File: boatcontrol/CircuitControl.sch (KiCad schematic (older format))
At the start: 3 parts, among them SW2601 ESB30, SW2602 ESB30

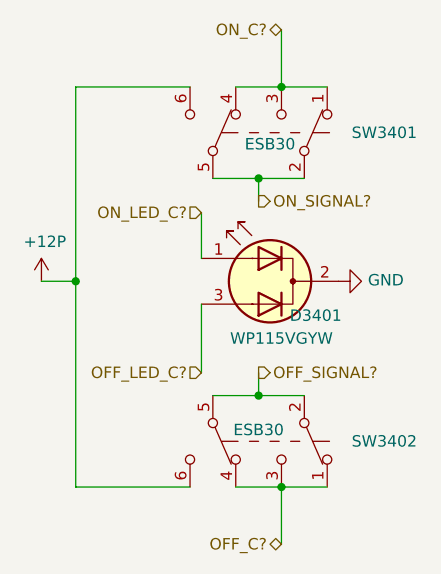
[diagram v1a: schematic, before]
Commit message: Fix extra signals
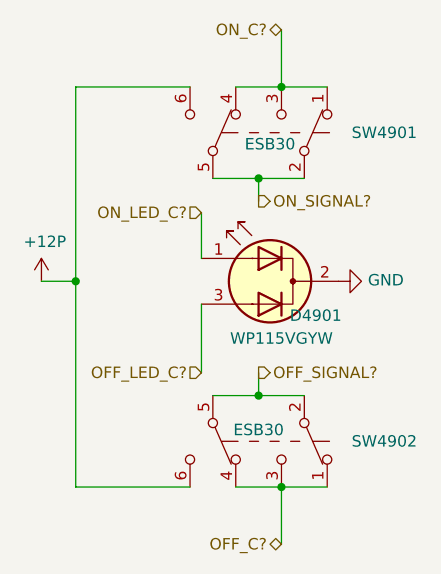
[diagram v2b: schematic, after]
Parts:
- renumbered D2601 to D4101, SW2601 to SW4101, SW2602 to SW4102
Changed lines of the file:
@@
 AR Path="/E0EE2714/E1383403/E15855D9/E150D6D7/E13B21A8" Ref="SW?"  Part="1"
 AR Path="/E0EE2714/E1383403/E15855D9/E150FD51/E13B21A8" Ref="SW?"  Part="1"
-AR Path="/E171B33C/E142CD30/E14BA326/E13B21A8" Ref="SW2602"  Part="1"
-AR Path="/E171B33C/E142CD30/E150AEB9/E13B21A8" Ref="SW2702"  Part="1"
-AR Path="/E171B33C/E142CD30/E150D6D7/E13B21A8" Ref="SW2802"  Part="1"
-AR Path="/E171B33C/E142CD30/E150FD51/E13B21A8" Ref="SW2902"  Part="1"
-AR Path="/E171B33C/E15855D9/E14BA326/E13B21A8" Ref="SW3102"  Part="1"
-AR Path="/E171B33C/E15855D9/E150AEB9/E13B21A8" Ref="SW3202"  Part="1"
-AR Path="/E171B33C/E15855D9/E150D6D7/E13B21A8" Ref="SW3302"  Part="1"
-AR Path="/E171B33C/E15855D9/E150FD51/E13B21A8" Ref="SW3402"  Part="1"
-F 0 "SW3402" V 5750 4250 50  0000 C CNN
+AR Path="/E171B33C/E142CD30/E14BA326/E13B21A8" Ref="SW4102"  Part="1"
+AR Path="/E171B33C/E142CD30/E150AEB9/E13B21A8" Ref="SW4202"  Part="1"
+AR Path="/E171B33C/E142CD30/E150D6D7/E13B21A8" Ref="SW4302"  Part="1"
+AR Path="/E171B33C/E142CD30/E150FD51/E13B21A8" Ref="SW4402"  Part="1"
+AR Path="/E171B33C/E15855D9/E14BA326/E13B21A8" Ref="SW4602"  Part="1"
+AR Path="/E171B33C/E15855D9/E150AEB9/E13B21A8" Ref="SW4702"  Part="1"
+AR Path="/E171B33C/E15855D9/E150D6D7/E13B21A8" Ref="SW4802"  Part="1"
+AR Path="/E171B33C/E15855D9/E150FD51/E13B21A8" Ref="SW4902"  Part="1"
+F 0 "SW4902" V 5750 4250 50  0000 C CNN
 F 1 " ESB30" V 5700 3700 50  0000 C CNN
 F 2 "BoatControl:SW_PUSH_ESB30_DPDT" H 5750 3900 50  0001 C CNN
@@
 AR Path="/E0EE2714/E1383403/E15855D9/E150D6D7/E13B21AE" Ref="#PWR?"  Part="1"
 AR Path="/E0EE2714/E1383403/E15855D9/E150FD51/E13B21AE" Ref="#PWR?"  Part="1"
-AR Path="/E171B33C/E142CD30/E14BA326/E13B21AE" Ref="#PWR02601"  Part="1"
-AR Path="/E171B33C/E142CD30/E150AEB9/E13B21AE" Ref="#PWR02701"  Part="1"
-AR Path="/E171B33C/E142CD30/E150D6D7/E13B21AE" Ref="#PWR02801"  Part="1"
-AR Path="/E171B33C/E142CD30/E150FD51/E13B21AE" Ref="#PWR02901"  Part="1"
-AR Path="/E171B33C/E15855D9/E14BA326/E13B21AE" Ref="#PWR03101"  Part="1"
-AR Path="/E171B33C/E15855D9/E150AEB9/E13B21AE" Ref="#PWR03201"  Part="1"
-AR Path="/E171B33C/E15855D9/E150D6D7/E13B21AE" Ref="#PWR03301"  Part="1"
-AR Path="/E171B33C/E15855D9/E150FD51/E13B21AE" Ref="#PWR03401"  Part="1"
-F 0 "#PWR03401" H 4800 2850 50  0001 C CNN
+AR Path="/E171B33C/E142CD30/E14BA326/E13B21AE" Ref="#PWR04101"  Part="1"
+AR Path="/E171B33C/E142CD30/E150AEB9/E13B21AE" Ref="#PWR04201"  Part="1"
+AR Path="/E171B33C/E142CD30/E150D6D7/E13B21AE" Ref="#PWR04301"  Part="1"
+AR Path="/E171B33C/E142CD30/E150FD51/E13B21AE" Ref="#PWR04401"  Part="1"
+AR Path="/E171B33C/E15855D9/E14BA326/E13B21AE" Ref="#PWR04601"  Part="1"
+AR Path="/E171B33C/E15855D9/E150AEB9/E13B21AE" Ref="#PWR04701"  Part="1"
+AR Path="/E171B33C/E15855D9/E150D6D7/E13B21AE" Ref="#PWR04801"  Part="1"
+AR Path="/E171B33C/E15855D9/E150FD51/E13B21AE" Ref="#PWR04901"  Part="1"
+F 0 "#PWR04901" H 4800 2850 50  0001 C CNN
 F 1 "+12P" H 4815 3173 50  0000 C CNN
 F 2 "" H 4800 3000 50  0001 C CNN
@@
 AR Path="/E0EE2714/E1383403/E15855D9/E150D6D7/E13B21B4" Ref="SW?"  Part="1"
 AR Path="/E0EE2714/E1383403/E15855D9/E150FD51/E13B21B4" Ref="SW?"  Part="1"
-AR Path="/E171B33C/E142CD30/E14BA326/E13B21B4" Ref="SW2601"  Part="1"
-AR Path="/E171B33C/E142CD30/E150AEB9/E13B21B4" Ref="SW2701"  Part="1"
-AR Path="/E171B33C/E142CD30/E150D6D7/E13B21B4" Ref="SW2801"  Part="1"
-AR Path="/E171B33C/E142CD30/E150FD51/E13B21B4" Ref="SW2901"  Part="1"
-AR Path="/E171B33C/E15855D9/E14BA326/E13B21B4" Ref="SW3101"  Part="1"
-AR Path="/E171B33C/E15855D9/E150AEB9/E13B21B4" Ref="SW3201"  Part="1"
-AR Path="/E171B33C/E15855D9/E150D6D7/E13B21B4" Ref="SW3301"  Part="1"
-AR Path="/E171B33C/E15855D9/E150FD51/E13B21B4" Ref="SW3401"  Part="1"
-F 0 "SW3401" V 5750 2900 50  0000 C CNN
+AR Path="/E171B33C/E142CD30/E14BA326/E13B21B4" Ref="SW4101"  Part="1"
+AR Path="/E171B33C/E142CD30/E150AEB9/E13B21B4" Ref="SW4201"  Part="1"
+AR Path="/E171B33C/E142CD30/E150D6D7/E13B21B4" Ref="SW4301"  Part="1"
+AR Path="/E171B33C/E142CD30/E150FD51/E13B21B4" Ref="SW4401"  Part="1"
+AR Path="/E171B33C/E15855D9/E14BA326/E13B21B4" Ref="SW4601"  Part="1"
+AR Path="/E171B33C/E15855D9/E150AEB9/E13B21B4" Ref="SW4701"  Part="1"
+AR Path="/E171B33C/E15855D9/E150D6D7/E13B21B4" Ref="SW4801"  Part="1"
+AR Path="/E171B33C/E15855D9/E150FD51/E13B21B4" Ref="SW4901"  Part="1"
+F 0 "SW4901" V 5750 2900 50  0000 C CNN
 F 1 " ESB30" V 5700 2400 50  0000 C CNN
 F 2 "BoatControl:SW_PUSH_ESB30_DPDT" H 5750 2550 50  0001 C CNN
@@
 AR Path="/E0EE2714/E1383403/E15855D9/E150D6D7/E13B21BC" Ref="D?"  Part="1"
 AR Path="/E0EE2714/E1383403/E15855D9/E150FD51/E13B21BC" Ref="D?"  Part="1"
-AR Path="/E171B33C/E142CD30/E14BA326/E13B21BC" Ref="D2601"  Part="1"
-AR Path="/E171B33C/E142CD30/E150AEB9/E13B21BC" Ref="D2701"  Part="1"
-AR Path="/E171B33C/E142CD30/E150D6D7/E13B21BC" Ref="D2801"  Part="1"
-AR Path="/E171B33C/E142CD30/E150FD51/E13B21BC" Ref="D2901"  Part="1"
-AR Path="/E171B33C/E15855D9/E14BA326/E13B21BC" Ref="D3101"  Part="1"
-AR Path="/E171B33C/E15855D9/E150AEB9/E13B21BC" Ref="D3201"  Part="1"
-AR Path="/E171B33C/E15855D9/E150D6D7/E13B21BC" Ref="D3301"  Part="1"
-AR Path="/E171B33C/E15855D9/E150FD51/E13B21BC" Ref="D3401"  Part="1"
-F 0 "D3401" H 5600 2850 50  0000 C CNN
+AR Path="/E171B33C/E142CD30/E14BA326/E13B21BC" Ref="D4101"  Part="1"
+AR Path="/E171B33C/E142CD30/E150AEB9/E13B21BC" Ref="D4201"  Part="1"
+AR Path="/E171B33C/E142CD30/E150D6D7/E13B21BC" Ref="D4301"  Part="1"
+AR Path="/E171B33C/E142CD30/E150FD51/E13B21BC" Ref="D4401"  Part="1"
+AR Path="/E171B33C/E15855D9/E14BA326/E13B21BC" Ref="D4601"  Part="1"
+AR Path="/E171B33C/E15855D9/E150AEB9/E13B21BC" Ref="D4701"  Part="1"
+AR Path="/E171B33C/E15855D9/E150D6D7/E13B21BC" Ref="D4801"  Part="1"
+AR Path="/E171B33C/E15855D9/E150FD51/E13B21BC" Ref="D4901"  Part="1"
+F 0 "D4901" H 5600 2850 50  0000 C CNN
 F 1 "WP115VGYW" H 5750 2750 50  0000 C CNN
 F 2 "LED_THT:LED_D5.0mm-3" H 5800 3000 50  0001 C CNN
@@
 	5750 3500 5550 3500
 $Comp
-L power:GND #PWR02602
+L power:GND #PWR04102
 U 1 1 5F521E18
 P 6100 3000
-AR Path="/E171B33C/E142CD30/E14BA326/5F521E18" Ref="#PWR02602"  Part="1"
-AR Path="/E171B33C/E142CD30/E150AEB9/5F521E18" Ref="#PWR02702"  Part="1"
-AR Path="/E171B33C/E142CD30/E150D6D7/5F521E18" Ref="#PWR02802"  Part="1"
-AR Path="/E171B33C/E142CD30/E150FD51/5F521E18" Ref="#PWR02902"  Part="1"
-AR Path="/E171B33C/E15855D9/E14BA326/5F521E18" Ref="#PWR03102"  Part="1"
-AR Path="/E171B33C/E15855D9/E150AEB9/5F521E18" Ref="#PWR03202"  Part="1"
-AR Path="/E171B33C/E15855D9/E150D6D7/5F521E18" Ref="#PWR03302"  Part="1"
-AR Path="/E171B33C/E15855D9/E150FD51/5F521E18" Ref="#PWR03402"  Part="1"
-F 0 "#PWR03402" H 6100 2750 50  0001 C CNN
+AR Path="/E171B33C/E142CD30/E14BA326/5F521E18" Ref="#PWR04102"  Part="1"
+AR Path="/E171B33C/E142CD30/E150AEB9/5F521E18" Ref="#PWR04202"  Part="1"
+AR Path="/E171B33C/E142CD30/E150D6D7/5F521E18" Ref="#PWR04302"  Part="1"
+AR Path="/E171B33C/E142CD30/E150FD51/5F521E18" Ref="#PWR04402"  Part="1"
+AR Path="/E171B33C/E15855D9/E14BA326/5F521E18" Ref="#PWR04602"  Part="1"
+AR Path="/E171B33C/E15855D9/E150AEB9/5F521E18" Ref="#PWR04702"  Part="1"
+AR Path="/E171B33C/E15855D9/E150D6D7/5F521E18" Ref="#PWR04802"  Part="1"
+AR Path="/E171B33C/E15855D9/E150FD51/5F521E18" Ref="#PWR04902"  Part="1"
+F 0 "#PWR04902" H 6100 2750 50  0001 C CNN
 F 1 "GND" V 6105 2872 50  0000 R CNN
 F 2 "" H 6100 3000 50  0001 C CNN

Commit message: Cleaner flow
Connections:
- net OFF_C? renamed DIG_OFF
- net OFF_LED_C? renamed OFF_LED
- net OFF_SIGNAL? renamed OFF
- net ON_C? renamed DIG_ON
- net ON_LED_C? renamed ON_LED
- net ON_SIGNAL? renamed ON
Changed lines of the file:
@@
 $Descr A4 11693 8268
 encoding utf-8
-Sheet 31 87
+Sheet 46 87
 Title "Boat Control Hat"
 Date "2020-07-09"
@@
 AR Path="/E171B33C/E15855D9/E150D6D7/E13B21A8" Ref="SW4802"  Part="1"
 AR Path="/E171B33C/E15855D9/E150FD51/E13B21A8" Ref="SW4902"  Part="1"
-F 0 "SW4902" V 5750 4250 50  0000 C CNN
+F 0 "SW4602" V 5750 4250 50  0000 C CNN
 F 1 " ESB30" V 5700 3700 50  0000 C CNN
 F 2 "BoatControl:SW_PUSH_ESB30_DPDT" H 5750 3900 50  0001 C CNN
@@
 AR Path="/E171B33C/E15855D9/E150D6D7/E13B21AE" Ref="#PWR04801"  Part="1"
 AR Path="/E171B33C/E15855D9/E150FD51/E13B21AE" Ref="#PWR04901"  Part="1"
-F 0 "#PWR04901" H 4800 2850 50  0001 C CNN
+F 0 "#PWR04601" H 4800 2850 50  0001 C CNN
 F 1 "+12P" H 4815 3173 50  0000 C CNN
 F 2 "" H 4800 3000 50  0001 C CNN
@@
 AR Path="/E171B33C/E15855D9/E150D6D7/E13B21B4" Ref="SW4801"  Part="1"
 AR Path="/E171B33C/E15855D9/E150FD51/E13B21B4" Ref="SW4901"  Part="1"
-F 0 "SW4901" V 5750 2900 50  0000 C CNN
+F 0 "SW4601" V 5750 2900 50  0000 C CNN
 F 1 " ESB30" V 5700 2400 50  0000 C CNN
 F 2 "BoatControl:SW_PUSH_ESB30_DPDT" H 5750 2550 50  0001 C CNN
@@
 AR Path="/E171B33C/E15855D9/E150D6D7/E13B21BC" Ref="D4801"  Part="1"
 AR Path="/E171B33C/E15855D9/E150FD51/E13B21BC" Ref="D4901"  Part="1"
-F 0 "D4901" H 5600 2850 50  0000 C CNN
+F 0 "D4601" H 5600 2850 50  0000 C CNN
 F 1 "WP115VGYW" H 5750 2750 50  0000 C CNN
 F 2 "LED_THT:LED_D5.0mm-3" H 5800 3000 50  0001 C CNN
@@
 $EndComp
 Text HLabel 5500 2700 0    50   Input ~ 0
-ON_LED_C?
+ON_LED
 Text HLabel 5500 3400 0    50   Input ~ 0
-OFF_LED_C?
+OFF_LED
 Text HLabel 5850 1900 0    50   BiDi ~ 0
-ON_C?
+DIG_ON
 Wire Wire Line
 	5850 1900 5850 2150
 Text HLabel 5850 4150 0    50   BiDi ~ 0
-OFF_C?
+DIG_OFF
 Wire Wire Line
 	5850 4150 5850 3900
 Text HLabel 5750 3400 2    50   Output ~ 0
-OFF_SIGNAL?
+OFF
 Text HLabel 5750 2650 2    50   Output ~ 0
-ON_SIGNAL?
+ON
 Wire Wire Line
 	5750 2650 5750 2550
@@
 AR Path="/E171B33C/E15855D9/E150D6D7/5F521E18" Ref="#PWR04802"  Part="1"
 AR Path="/E171B33C/E15855D9/E150FD51/5F521E18" Ref="#PWR04902"  Part="1"
-F 0 "#PWR04902" H 6100 2750 50  0001 C CNN
+F 0 "#PWR04602" H 6100 2750 50  0001 C CNN
 F 1 "GND" V 6105 2872 50  0000 R CNN
 F 2 "" H 6100 3000 50  0001 C CNN

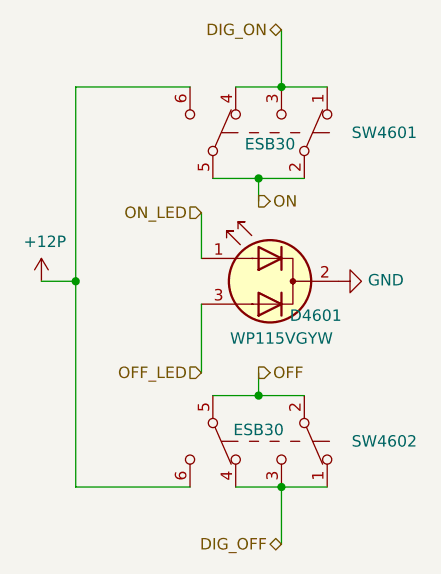
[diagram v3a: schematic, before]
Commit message: Change inductors
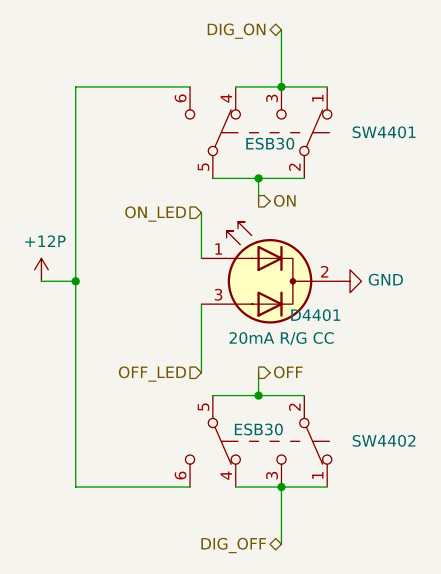
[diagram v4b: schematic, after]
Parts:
- D4101: value WP115VGYW -> 20mA R/G CC; Manufacturer (none) -> Kingbright; Model (none) -> WP59EGW
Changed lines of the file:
@@
 $Descr A4 11693 8268
 encoding utf-8
-Sheet 46 87
+Sheet 43 87
 Title "Boat Control Hat"
 Date "2020-07-09"
@@
 AR Path="/E171B33C/E15855D9/E150D6D7/E13B21A8" Ref="SW4802"  Part="1"
 AR Path="/E171B33C/E15855D9/E150FD51/E13B21A8" Ref="SW4902"  Part="1"
-F 0 "SW4602" V 5750 4250 50  0000 C CNN
+F 0 "SW4402" V 5750 4250 50  0000 C CNN
 F 1 " ESB30" V 5700 3700 50  0000 C CNN
 F 2 "BoatControl:SW_PUSH_ESB30_DPDT" H 5750 3900 50  0001 C CNN
@@
 AR Path="/E171B33C/E15855D9/E150D6D7/E13B21AE" Ref="#PWR04801"  Part="1"
 AR Path="/E171B33C/E15855D9/E150FD51/E13B21AE" Ref="#PWR04901"  Part="1"
-F 0 "#PWR04601" H 4800 2850 50  0001 C CNN
+F 0 "#PWR04401" H 4800 2850 50  0001 C CNN
 F 1 "+12P" H 4815 3173 50  0000 C CNN
 F 2 "" H 4800 3000 50  0001 C CNN
@@
 AR Path="/E171B33C/E15855D9/E150D6D7/E13B21B4" Ref="SW4801"  Part="1"
 AR Path="/E171B33C/E15855D9/E150FD51/E13B21B4" Ref="SW4901"  Part="1"
-F 0 "SW4601" V 5750 2900 50  0000 C CNN
+F 0 "SW4401" V 5750 2900 50  0000 C CNN
 F 1 " ESB30" V 5700 2400 50  0000 C CNN
 F 2 "BoatControl:SW_PUSH_ESB30_DPDT" H 5750 2550 50  0001 C CNN
@@
 AR Path="/E171B33C/E15855D9/E150D6D7/E13B21BC" Ref="D4801"  Part="1"
 AR Path="/E171B33C/E15855D9/E150FD51/E13B21BC" Ref="D4901"  Part="1"
-F 0 "D4601" H 5600 2850 50  0000 C CNN
-F 1 "WP115VGYW" H 5750 2750 50  0000 C CNN
+F 0 "D4401" H 5600 2850 50  0000 C CNN
+F 1 "20mA R/G CC" H 5750 2750 50  0000 C CNN
 F 2 "LED_THT:LED_D5.0mm-3" H 5800 3000 50  0001 C CNN
-F 3 "https://www.mouser.ca/datasheet/2/216/WP115VGYW-232005.pdf" H 5800 3000 50  0001 C CNN
+F 3 "http://www.kingbrightusa.com/images/catalog/SPEC/WP59EGW.pdf" H 5800 3000 50  0001 C CNN
+F 4 "WP59EGW" H 5800 3000 50  0001 C CNN "Model"
+F 5 "Kingbright" H 5800 3000 50  0001 C CNN "Manufacturer"
 	1    5800 3000
 	-1   0    0    -1
@@
 AR Path="/E171B33C/E15855D9/E150D6D7/5F521E18" Ref="#PWR04802"  Part="1"
 AR Path="/E171B33C/E15855D9/E150FD51/5F521E18" Ref="#PWR04902"  Part="1"
-F 0 "#PWR04602" H 6100 2750 50  0001 C CNN
+F 0 "#PWR04402" H 6100 2750 50  0001 C CNN
 F 1 "GND" V 6105 2872 50  0000 R CNN
 F 2 "" H 6100 3000 50  0001 C CNN

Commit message: CRC ErrorFree
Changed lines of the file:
@@
 $Descr A4 11693 8268
 encoding utf-8
-Sheet 43 87
+Sheet 46 87
 Title "Boat Control Hat"
 Date "2020-07-09"
@@
 AR Path="/E0EE2714/E1383403/E15855D9/E150FD51/E13B21A8" Ref="SW?"  Part="1"
 AR Path="/E171B33C/E142CD30/E14BA326/E13B21A8" Ref="SW4102"  Part="1"
-AR Path="/E171B33C/E142CD30/E150AEB9/E13B21A8" Ref="SW4202"  Part="1"
-AR Path="/E171B33C/E142CD30/E150D6D7/E13B21A8" Ref="SW4302"  Part="1"
-AR Path="/E171B33C/E142CD30/E150FD51/E13B21A8" Ref="SW4402"  Part="1"
+AR Path="/E171B33C/E142CD30/E150AEB9/E13B21A8" Ref="SW4402"  Part="1"
+AR Path="/E171B33C/E142CD30/E150D6D7/E13B21A8" Ref="SW4202"  Part="1"
+AR Path="/E171B33C/E142CD30/E150FD51/E13B21A8" Ref="SW4302"  Part="1"
 AR Path="/E171B33C/E15855D9/E14BA326/E13B21A8" Ref="SW4602"  Part="1"
-AR Path="/E171B33C/E15855D9/E150AEB9/E13B21A8" Ref="SW4702"  Part="1"
-AR Path="/E171B33C/E15855D9/E150D6D7/E13B21A8" Ref="SW4802"  Part="1"
-AR Path="/E171B33C/E15855D9/E150FD51/E13B21A8" Ref="SW4902"  Part="1"
-F 0 "SW4402" V 5750 4250 50  0000 C CNN
+AR Path="/E171B33C/E15855D9/E150AEB9/E13B21A8" Ref="SW4902"  Part="1"
+AR Path="/E171B33C/E15855D9/E150D6D7/E13B21A8" Ref="SW4702"  Part="1"
+AR Path="/E171B33C/E15855D9/E150FD51/E13B21A8" Ref="SW4802"  Part="1"
+F 0 "SW4902" V 5750 4250 50  0000 C CNN
 F 1 " ESB30" V 5700 3700 50  0000 C CNN
 F 2 "BoatControl:SW_PUSH_ESB30_DPDT" H 5750 3900 50  0001 C CNN
@@
 AR Path="/E0EE2714/E1383403/E15855D9/E150FD51/E13B21AE" Ref="#PWR?"  Part="1"
 AR Path="/E171B33C/E142CD30/E14BA326/E13B21AE" Ref="#PWR04101"  Part="1"
-AR Path="/E171B33C/E142CD30/E150AEB9/E13B21AE" Ref="#PWR04201"  Part="1"
-AR Path="/E171B33C/E142CD30/E150D6D7/E13B21AE" Ref="#PWR04301"  Part="1"
-AR Path="/E171B33C/E142CD30/E150FD51/E13B21AE" Ref="#PWR04401"  Part="1"
+AR Path="/E171B33C/E142CD30/E150AEB9/E13B21AE" Ref="#PWR04401"  Part="1"
+AR Path="/E171B33C/E142CD30/E150D6D7/E13B21AE" Ref="#PWR04201"  Part="1"
+AR Path="/E171B33C/E142CD30/E150FD51/E13B21AE" Ref="#PWR04301"  Part="1"
 AR Path="/E171B33C/E15855D9/E14BA326/E13B21AE" Ref="#PWR04601"  Part="1"
-AR Path="/E171B33C/E15855D9/E150AEB9/E13B21AE" Ref="#PWR04701"  Part="1"
-AR Path="/E171B33C/E15855D9/E150D6D7/E13B21AE" Ref="#PWR04801"  Part="1"
-AR Path="/E171B33C/E15855D9/E150FD51/E13B21AE" Ref="#PWR04901"  Part="1"
-F 0 "#PWR04401" H 4800 2850 50  0001 C CNN
+AR Path="/E171B33C/E15855D9/E150AEB9/E13B21AE" Ref="#PWR04901"  Part="1"
+AR Path="/E171B33C/E15855D9/E150D6D7/E13B21AE" Ref="#PWR04701"  Part="1"
+AR Path="/E171B33C/E15855D9/E150FD51/E13B21AE" Ref="#PWR04801"  Part="1"
+F 0 "#PWR04901" H 4800 2850 50  0001 C CNN
 F 1 "+12P" H 4815 3173 50  0000 C CNN
 F 2 "" H 4800 3000 50  0001 C CNN
@@
 AR Path="/E0EE2714/E1383403/E15855D9/E150FD51/E13B21B4" Ref="SW?"  Part="1"
 AR Path="/E171B33C/E142CD30/E14BA326/E13B21B4" Ref="SW4101"  Part="1"
-AR Path="/E171B33C/E142CD30/E150AEB9/E13B21B4" Ref="SW4201"  Part="1"
-AR Path="/E171B33C/E142CD30/E150D6D7/E13B21B4" Ref="SW4301"  Part="1"
-AR Path="/E171B33C/E142CD30/E150FD51/E13B21B4" Ref="SW4401"  Part="1"
+AR Path="/E171B33C/E142CD30/E150AEB9/E13B21B4" Ref="SW4401"  Part="1"
+AR Path="/E171B33C/E142CD30/E150D6D7/E13B21B4" Ref="SW4201"  Part="1"
+AR Path="/E171B33C/E142CD30/E150FD51/E13B21B4" Ref="SW4301"  Part="1"
 AR Path="/E171B33C/E15855D9/E14BA326/E13B21B4" Ref="SW4601"  Part="1"
-AR Path="/E171B33C/E15855D9/E150AEB9/E13B21B4" Ref="SW4701"  Part="1"
-AR Path="/E171B33C/E15855D9/E150D6D7/E13B21B4" Ref="SW4801"  Part="1"
-AR Path="/E171B33C/E15855D9/E150FD51/E13B21B4" Ref="SW4901"  Part="1"
-F 0 "SW4401" V 5750 2900 50  0000 C CNN
+AR Path="/E171B33C/E15855D9/E150AEB9/E13B21B4" Ref="SW4901"  Part="1"
+AR Path="/E171B33C/E15855D9/E150D6D7/E13B21B4" Ref="SW4701"  Part="1"
+AR Path="/E171B33C/E15855D9/E150FD51/E13B21B4" Ref="SW4801"  Part="1"
+F 0 "SW4901" V 5750 2900 50  0000 C CNN
 F 1 " ESB30" V 5700 2400 50  0000 C CNN
 F 2 "BoatControl:SW_PUSH_ESB30_DPDT" H 5750 2550 50  0001 C CNN
@@
 AR Path="/E0EE2714/E1383403/E15855D9/E150FD51/E13B21BC" Ref="D?"  Part="1"
 AR Path="/E171B33C/E142CD30/E14BA326/E13B21BC" Ref="D4101"  Part="1"
-AR Path="/E171B33C/E142CD30/E150AEB9/E13B21BC" Ref="D4201"  Part="1"
-AR Path="/E171B33C/E142CD30/E150D6D7/E13B21BC" Ref="D4301"  Part="1"
-AR Path="/E171B33C/E142CD30/E150FD51/E13B21BC" Ref="D4401"  Part="1"
+AR Path="/E171B33C/E142CD30/E150AEB9/E13B21BC" Ref="D4401"  Part="1"
+AR Path="/E171B33C/E142CD30/E150D6D7/E13B21BC" Ref="D4201"  Part="1"
+AR Path="/E171B33C/E142CD30/E150FD51/E13B21BC" Ref="D4301"  Part="1"
 AR Path="/E171B33C/E15855D9/E14BA326/E13B21BC" Ref="D4601"  Part="1"
-AR Path="/E171B33C/E15855D9/E150AEB9/E13B21BC" Ref="D4701"  Part="1"
-AR Path="/E171B33C/E15855D9/E150D6D7/E13B21BC" Ref="D4801"  Part="1"
-AR Path="/E171B33C/E15855D9/E150FD51/E13B21BC" Ref="D4901"  Part="1"
-F 0 "D4401" H 5600 2850 50  0000 C CNN
+AR Path="/E171B33C/E15855D9/E150AEB9/E13B21BC" Ref="D4901"  Part="1"
+AR Path="/E171B33C/E15855D9/E150D6D7/E13B21BC" Ref="D4701"  Part="1"
+AR Path="/E171B33C/E15855D9/E150FD51/E13B21BC" Ref="D4801"  Part="1"
+F 0 "D4901" H 5600 2850 50  0000 C CNN
 F 1 "20mA R/G CC" H 5750 2750 50  0000 C CNN
 F 2 "LED_THT:LED_D5.0mm-3" H 5800 3000 50  0001 C CNN
@@
 P 6100 3000
 AR Path="/E171B33C/E142CD30/E14BA326/5F521E18" Ref="#PWR04102"  Part="1"
-AR Path="/E171B33C/E142CD30/E150AEB9/5F521E18" Ref="#PWR04202"  Part="1"
-AR Path="/E171B33C/E142CD30/E150D6D7/5F521E18" Ref="#PWR04302"  Part="1"
-AR Path="/E171B33C/E142CD30/E150FD51/5F521E18" Ref="#PWR04402"  Part="1"
+AR Path="/E171B33C/E142CD30/E150AEB9/5F521E18" Ref="#PWR04402"  Part="1"
+AR Path="/E171B33C/E142CD30/E150D6D7/5F521E18" Ref="#PWR04202"  Part="1"
+AR Path="/E171B33C/E142CD30/E150FD51/5F521E18" Ref="#PWR04302"  Part="1"
 AR Path="/E171B33C/E15855D9/E14BA326/5F521E18" Ref="#PWR04602"  Part="1"
-AR Path="/E171B33C/E15855D9/E150AEB9/5F521E18" Ref="#PWR04702"  Part="1"
-AR Path="/E171B33C/E15855D9/E150D6D7/5F521E18" Ref="#PWR04802"  Part="1"
-AR Path="/E171B33C/E15855D9/E150FD51/5F521E18" Ref="#PWR04902"  Part="1"
-F 0 "#PWR04402" H 6100 2750 50  0001 C CNN
+AR Path="/E171B33C/E15855D9/E150AEB9/5F521E18" Ref="#PWR04902"  Part="1"
+AR Path="/E171B33C/E15855D9/E150D6D7/5F521E18" Ref="#PWR04702"  Part="1"
+AR Path="/E171B33C/E15855D9/E150FD51/5F521E18" Ref="#PWR04802"  Part="1"
+F 0 "#PWR04902" H 6100 2750 50  0001 C CNN
 F 1 "GND" V 6105 2872 50  0000 R CNN
 F 2 "" H 6100 3000 50  0001 C CNN
